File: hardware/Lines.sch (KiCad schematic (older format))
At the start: 32 parts, among them K10 L4_COIN_CTRL, K3 L1_HOLD, K4 L1_COIN_CTRL, K5 L2_HOLD, K6 L2_COIN_CTRL, K7 L3_HOLD, K8 L3_COIN_CTRL, K9 L4_HOLD, U10 H11AA1, U7 H11AA1, U8 H11AA1, U9 H11AA1

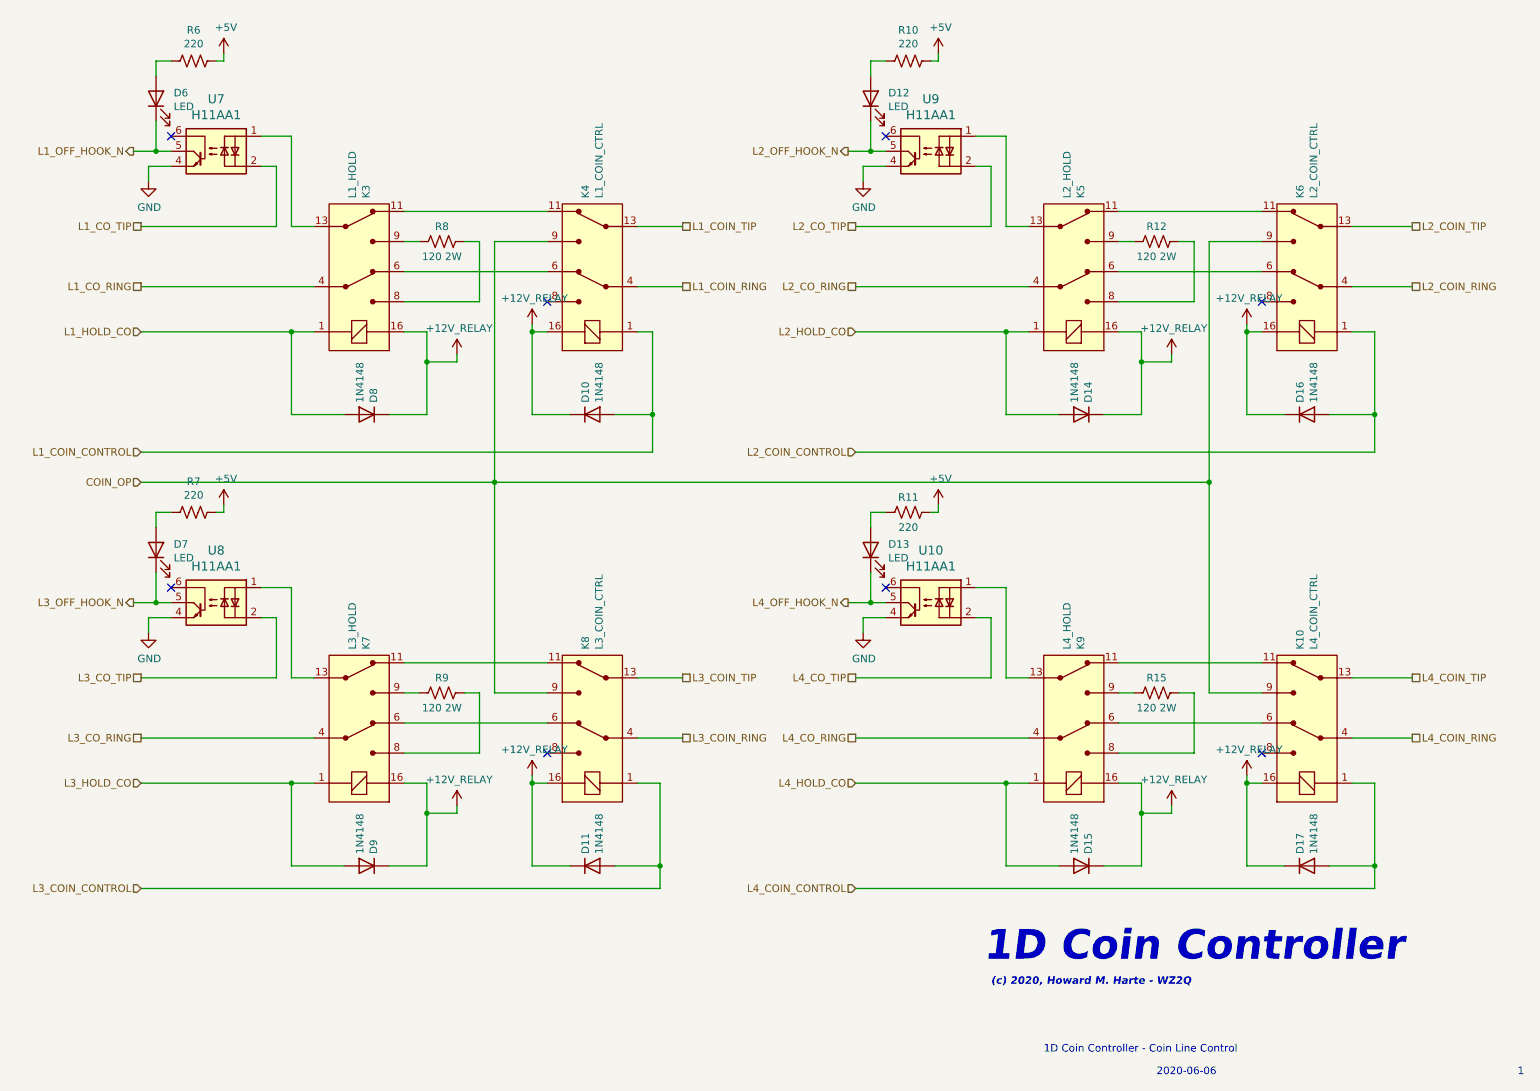
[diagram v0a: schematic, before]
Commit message: Issue 2 schmatic and Layout
Added polarity reversal detection to monitor answer supervision.
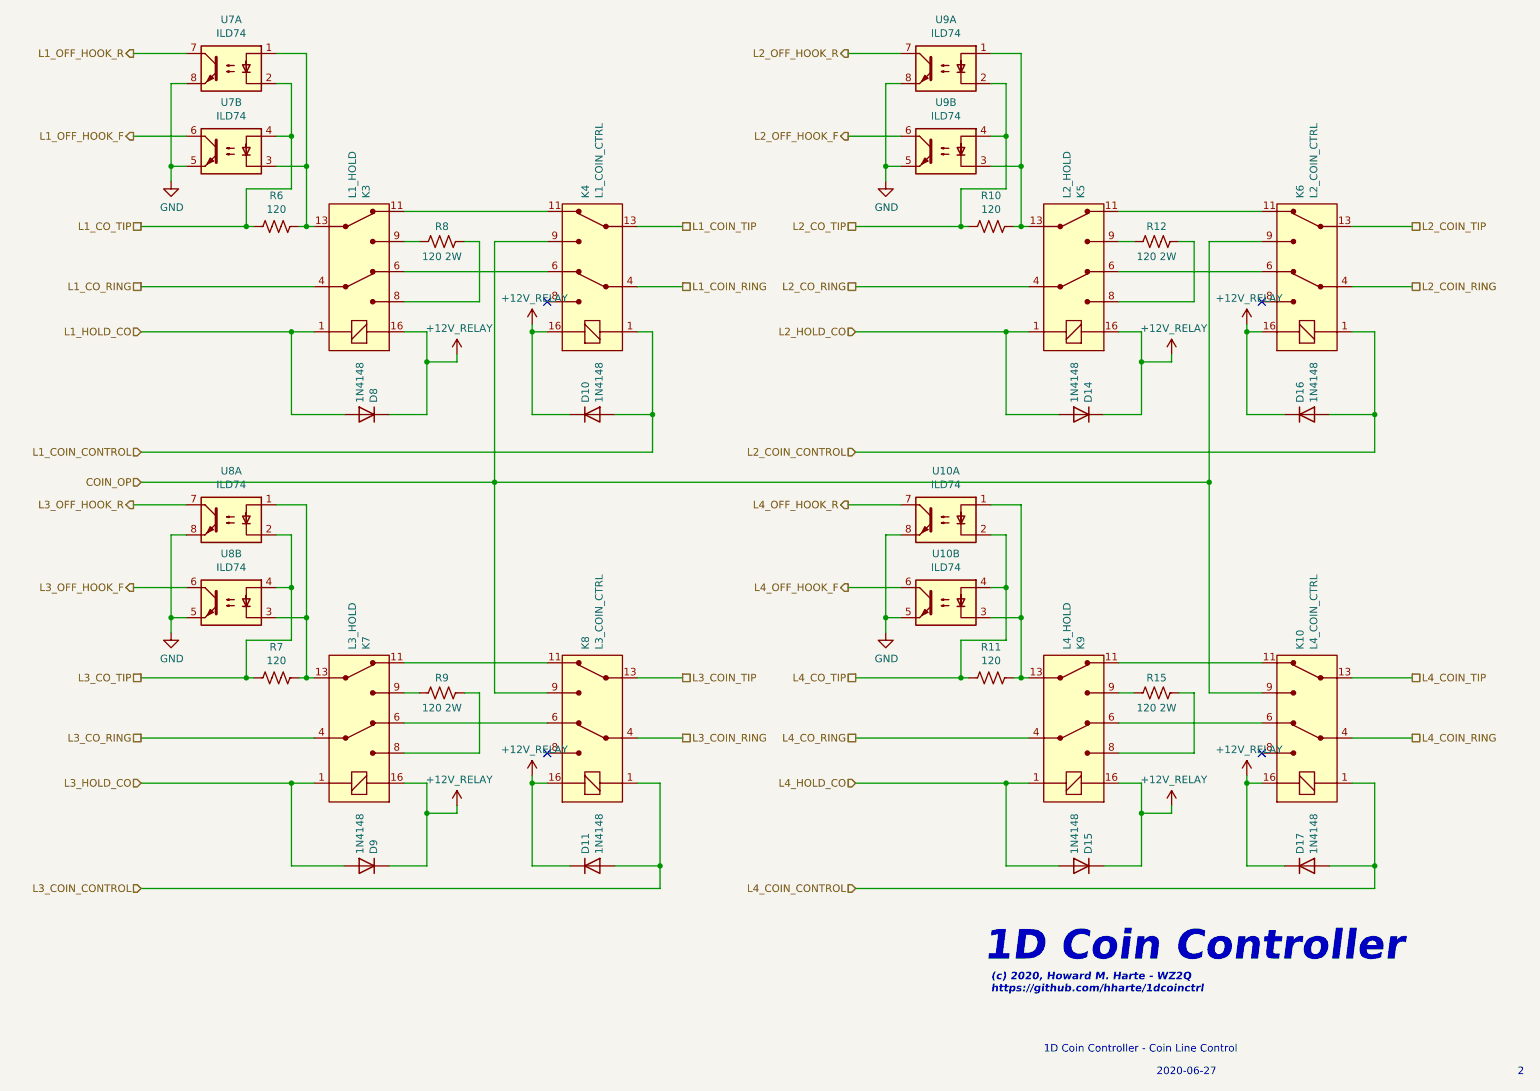
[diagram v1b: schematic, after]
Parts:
- removed D12, D13, D6, D7: LED, LED_THT:LED_D5.0mm, symbol Device:LED
- removed U10, U7, U8, U9: H11AA1, Package_DIP:DIP-6_W7.62mm, symbol Isolator:H11AA1
- added U10, U7, U8, U9: ILD74, Package_DIP:DIP-8_W7.62mm_Socket, symbol Isolator:ILD74
- R10, R11, R6, R7: value 220 -> 120
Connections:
- net GND: now also U10.5, U10.8, U7.5, U7.8, U8.5, U8.8, U9.5, U9.8
- net L1_CO_TIP: now also R6.2, U7.2, U7.4
- net L2_CO_TIP: now also R10.2, U9.2, U9.4
- net L3_CO_TIP: now also R7.2, U8.2, U8.4
- net L4_CO_TIP: now also R11.2, U10.2, U10.4
- net at K3.13 (COM2): now also R6.1, U7.1, U7.3
- net at K5.13 (COM2): now also R10.1, U9.1, U9.3
- net at K7.13 (COM2): now also R7.1, U8.1, U8.3
- net at K9.13 (COM2): now also R11.1, U10.1, U10.3
- removed net +5V: R10.1, R11.1, R6.1, R7.1
- new net L1_OFF_HOOK_F: U7.6
- new net L1_OFF_HOOK_R: U7.7
- new net L2_OFF_HOOK_F: U9.6
- new net L2_OFF_HOOK_R: U9.7
- new net L3_OFF_HOOK_F: U8.6
- new net L3_OFF_HOOK_R: U8.7
- new net L4_OFF_HOOK_F: U10.6
- new net L4_OFF_HOOK_R: U10.7
- no-connect marks 8 -> 4
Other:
- note added: "(c) 2020, Howard M. Harte - WZ2Q\nhttps://github.com/hharte/1dcoinctrl"
- note added: "2"
- note added: "2020-06-27"
- note removed: "(c) 2020, Howard M. Harte - WZ2Q"
- note removed: "1"
- note removed: "2020-06-06"
